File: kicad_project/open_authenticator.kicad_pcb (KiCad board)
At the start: 2 copper layers, 82 x 42 mm, 64 parts, among them IC1 TPS22919DCKR, J1 Conn_01x02_Female, J2 TYPE-C-31-M-17, J3 Conn_01x02_Female, P1 SSD1306_ribbon, Q1 DMP2305U-7, SW1 UP, SW2 DOWN, SW3 BOOT/SELECT, SW4 RESET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

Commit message: Updated silkscreen with symbols, and a bit of art
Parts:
- added ?: , buzzard_labels, F.Cu at (149.0, 117.4)
- added ?: , buzzard_labels, F.Cu at (134.4, 117.4)
- added ?: , buzzard_labels, F.Cu at (124.1, 117.4)
- added ?: , buzzard_labels, F.Cu at (111.7, 117.4)
- added ?: , buzzard_labels, F.Cu at (166.1, 111.5)
- added ?: , buzzard_labels, F.Cu at (166.4, 101.2)
- added ?: , buzzard_labels, F.Cu at (115.0, 95.8)
- added ?: , buzzard_labels, F.Cu at (115.0, 88.8)
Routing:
- net GND: track 213.1 -> 205.0 mm
- net /A1_7_BATT: track 32.5 -> 35.2 mm
- net +3V3: track 139.4 -> 138.2 mm, vias 19 -> 21
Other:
- board text added: "Boot + Reset to flash"
- board text added: "ESP32"
- board text added: "Selects which power source to use"
- board text added: "USB-C"
- board text added: "WiFi Module"
- board text removed: "OFF"
- board text removed: "ON"
- board text removed: "RX"
- board text removed: "TX"

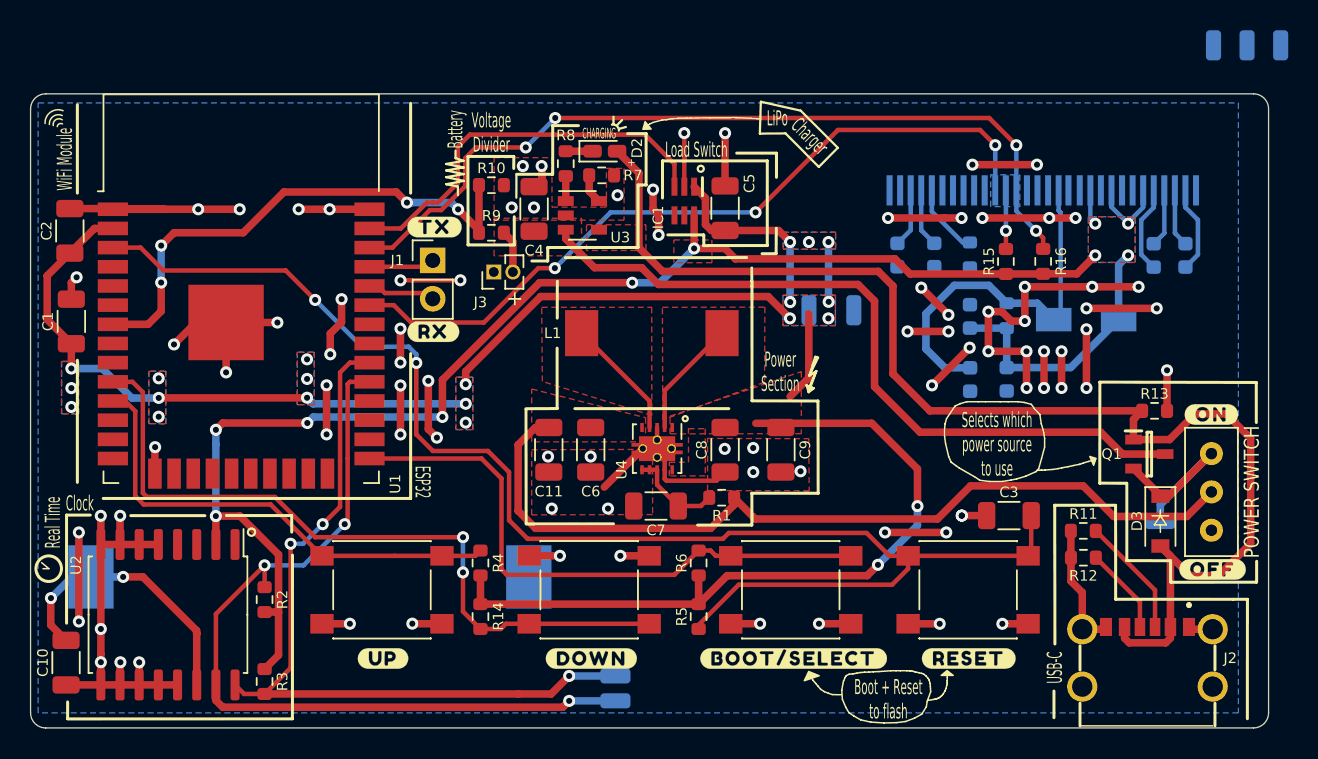
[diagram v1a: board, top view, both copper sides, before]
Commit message: Completed work on F.Cu Layer and F.Silk
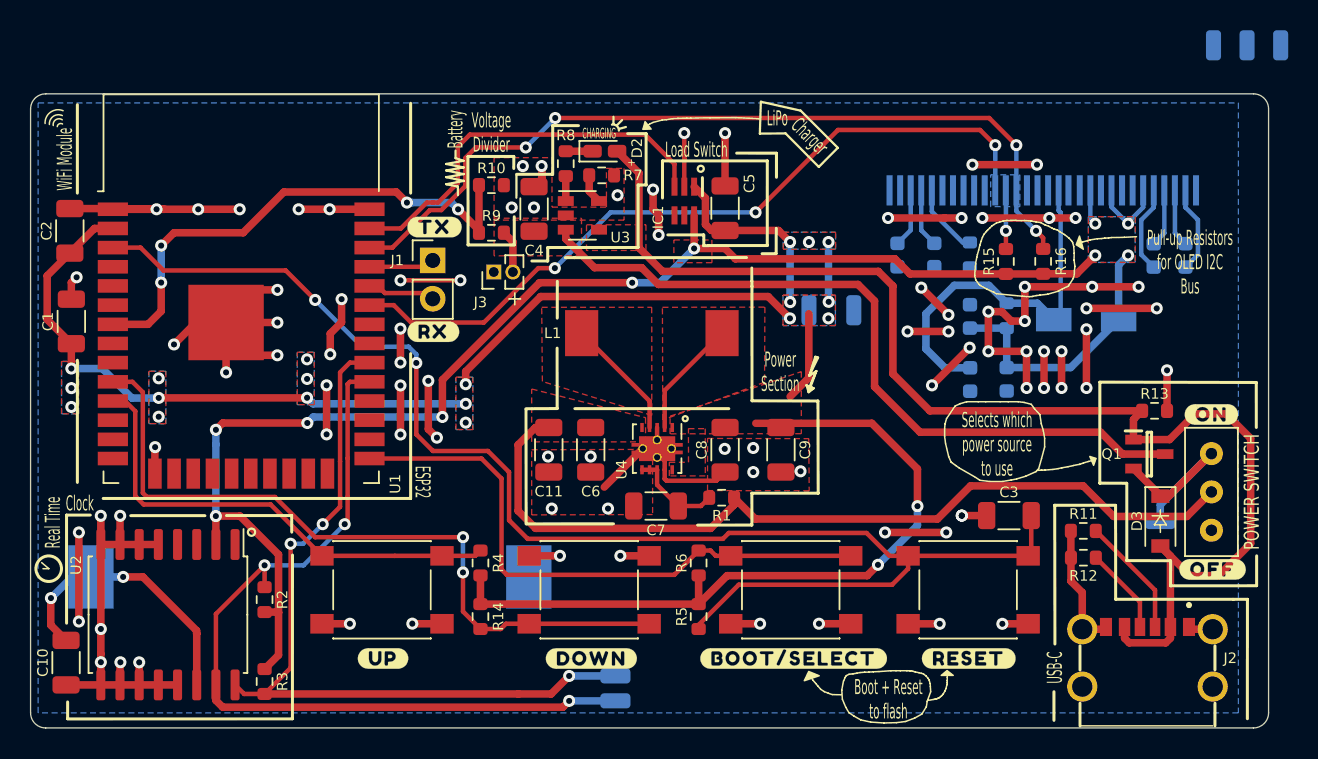
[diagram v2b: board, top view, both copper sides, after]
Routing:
- net GND: track 205.0 -> 214.0 mm, vias 88 -> 91
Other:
- board text added: "Pull-up Resistors for OLED I2C Bus"

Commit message: Placed mounting holes on the board
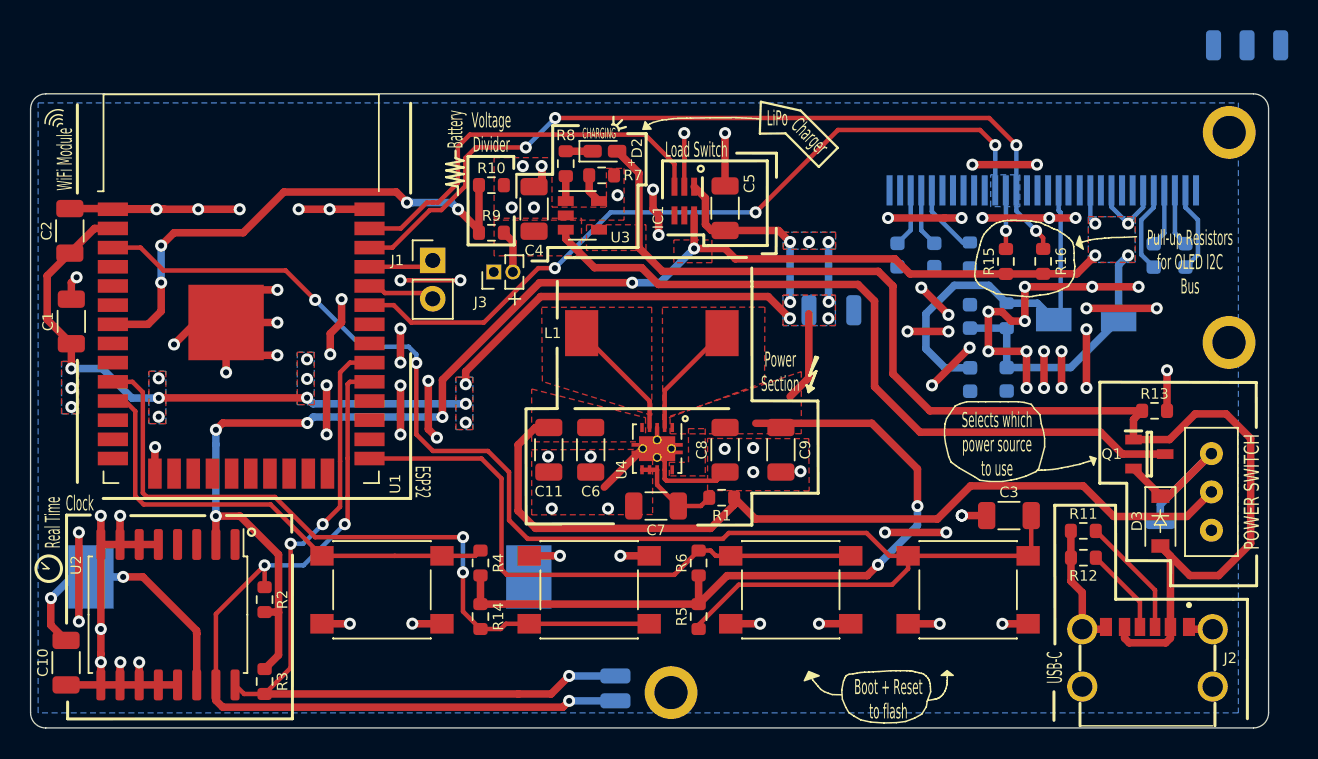
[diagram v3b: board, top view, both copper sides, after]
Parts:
- removed ? (x8): , buzzard_labels
- added H1: MountingHole_Pad, MountingHole:MountingHole_2.2mm_M2_ISO7380_Pad, F.Cu at (169.4, 82.6)
- added H2: MountingHole_Pad, MountingHole:MountingHole_2.2mm_M2_ISO7380_Pad, F.Cu at (169.4, 96.5)
- added H3: MountingHole_Pad, MountingHole:MountingHole_2.2mm_M2_ISO7380_Pad, F.Cu at (132.4, 119.7)

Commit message: ad
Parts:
- added ?: , buzzard_labels, F.Cu at (114.8, 88.8)
- added ?: , buzzard_labels, B.Cu at (141.5, 99.8)
- added ?: , buzzard_labels, B.Cu at (163.2, 108.3)
- added ?: , buzzard_labels, B.Cu at (125.1, 120.2)
- added ?: , buzzard_labels, B.Cu at (125.1, 118.6)
- added ?: , buzzard_labels, F.Cu at (114.9, 95.9)
- added ?: , buzzard_labels, F.Cu at (166.1, 111.6)
- added ?: , buzzard_labels, F.Cu at (166.5, 101.1)
- added ?: , buzzard_labels, F.Cu at (149.0, 117.2)
- added ?: , buzzard_labels, F.Cu at (134.2, 117.2)
- added ?: , buzzard_labels, F.Cu at (124.0, 117.2)
- added ?: , buzzard_labels, F.Cu at (111.6, 117.2)
- added ?: , buzzard_labels, B.Cu at (144.5, 100.0)
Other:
- board text added: "Backup Power for RTC"
- board text added: "CR2032"

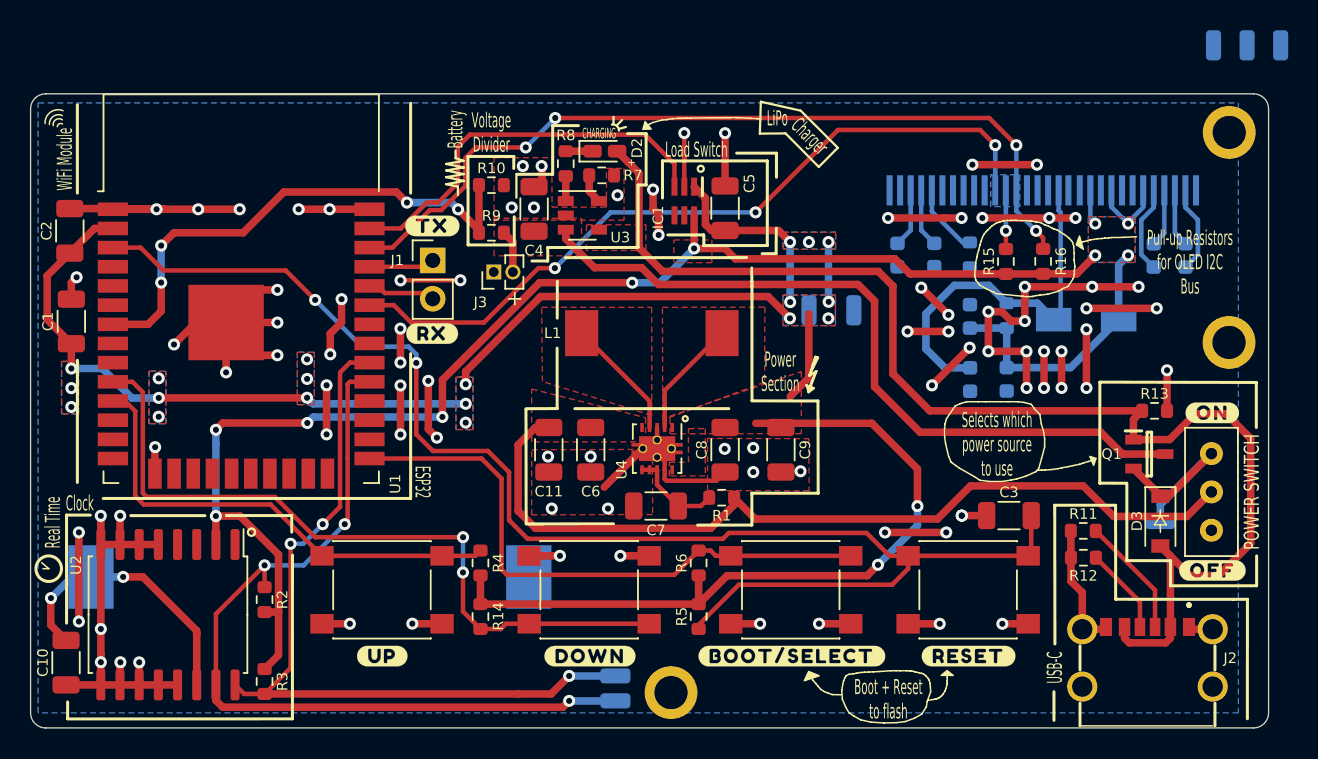
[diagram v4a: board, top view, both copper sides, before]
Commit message: Finished cleaning up bottom layer, silkscreen also updated
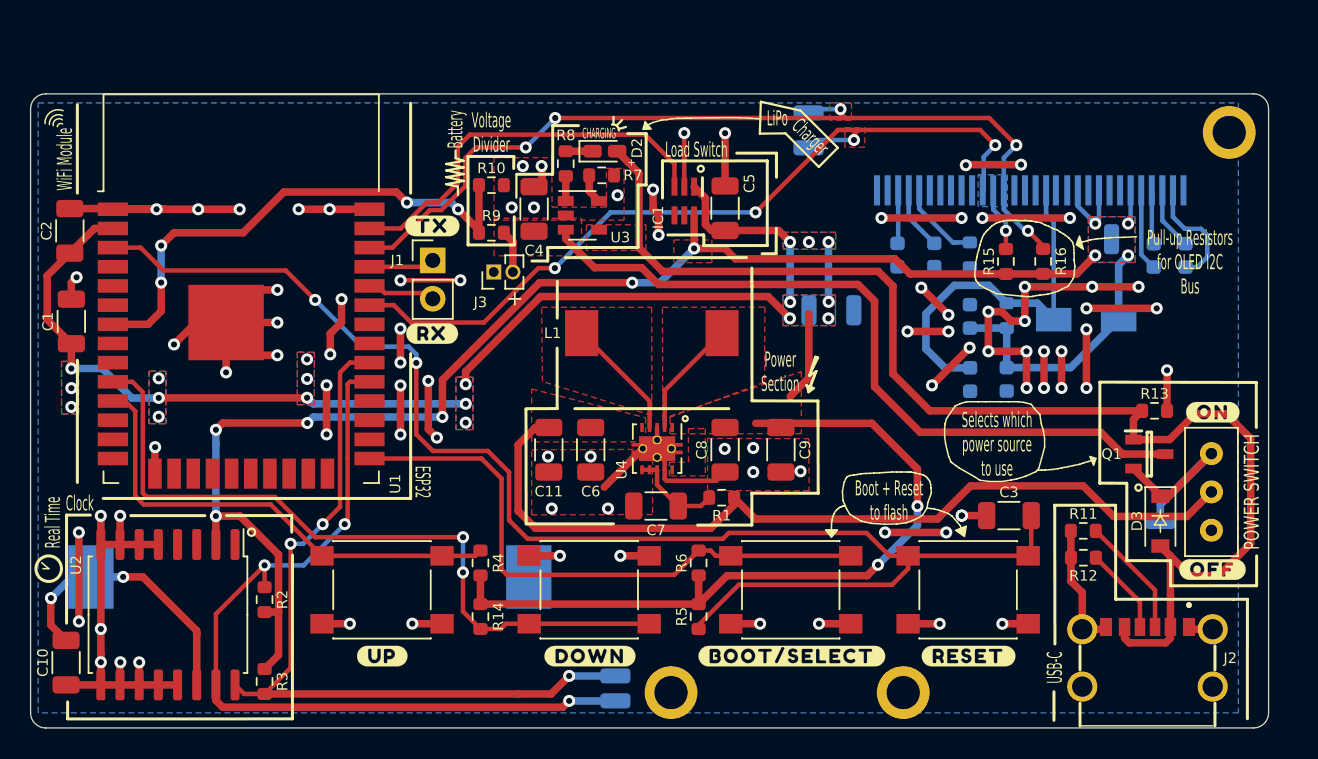
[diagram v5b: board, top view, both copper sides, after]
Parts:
- added ?: , buzzard_labels, B.Cu at (140.2, 83.6)
- added ?: , buzzard_labels, B.Cu at (140.2, 81.3)
- added ?: , buzzard_labels, B.Cu at (161.0, 89.6)
- added REF**: WEEE-Logo_4.2x6mm_SilkScreen, Symbol:WEEE-Logo_4.2x6mm_SilkScreen, B.Cu at (164.0, 117.2)
- added REF**: KiCad-Logo2_5mm_SilkScreen, Symbol:KiCad-Logo2_5mm_SilkScreen, B.Cu at (104.6, 83.2)
- added REF**: OSHW-Logo2_7.3x6mm_SilkScreen, Symbol:OSHW-Logo2_7.3x6mm_SilkScreen, B.Cu at (93.7, 83.4)
- moved H2 31.7 mm to (147.8, 119.7)
- moved TP6 29.8 mm to (141.5, 83.6), turned to 270 degrees
- moved TP7 27.2 mm to (141.5, 81.3), turned to 270 degrees
- moved TP4 17.0 mm to (161.6, 89.6)
- moved P1 0.83 mm to (156.2, 86.4)
- moved ? 0.06 mm to (166.1, 111.5)
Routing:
- net /IO21_SDA: track 54.5 -> 59.2 mm, vias 4 -> 5
- net /IO22_SCL: track 55.8 -> 59.6 mm, vias 4 -> 5
- net Net-(C17-Pad1): track 5.76 -> 7.70 mm
- net Net-(P1-Pad26): track 4.77 -> 5.50 mm
- net Net-(C14-Pad2): track 24.8 -> 25.4 mm
- net GND: track 214.0 -> 213.4 mm, vias 91 -> 90
- added copper zone on F.Cu, net /IO21_SDA
- added copper zone on F.Cu, net /IO22_SCL
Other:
- board text added: "SSD1306 OLED Section"
- board text removed: "Open Authenticator"
- board text removed: "v1.3 Vedant Paranjape"

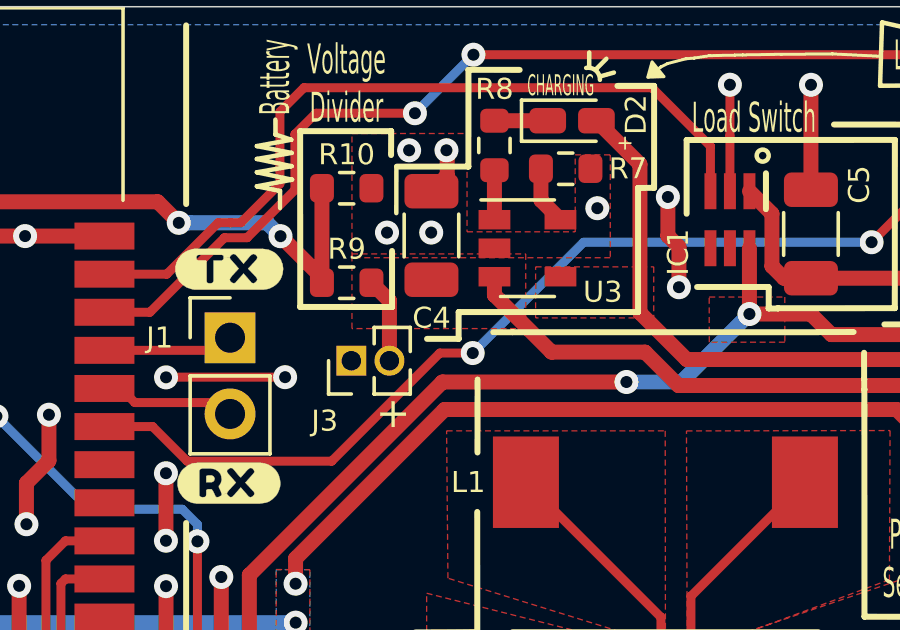
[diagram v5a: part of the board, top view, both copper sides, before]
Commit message: Added lipo connector to board and placed it accordingly
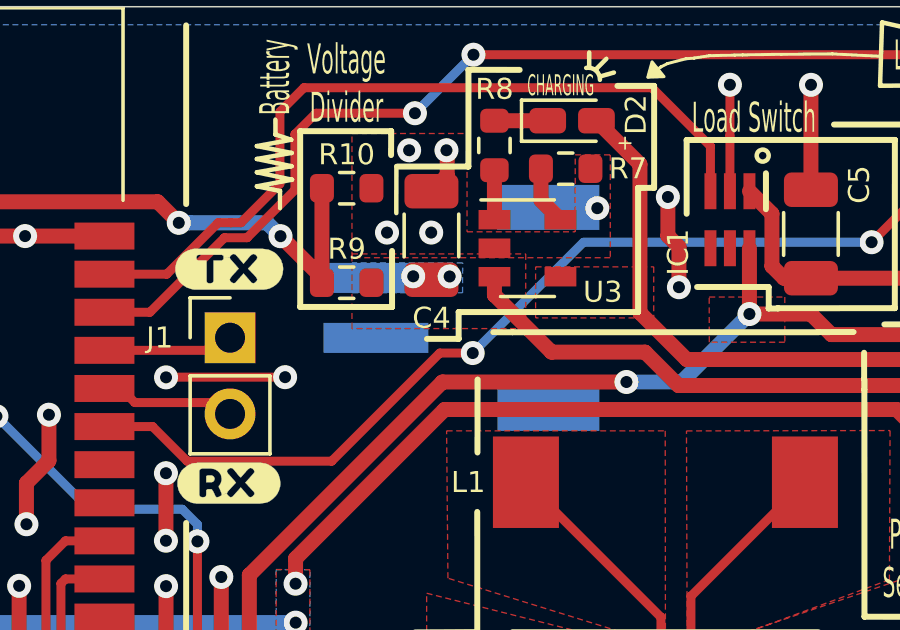
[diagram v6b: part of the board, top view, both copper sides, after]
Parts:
- J3: value Conn_01x02_Female -> S2B-PH-SM4-TB(LF)(SN); footprint Connector_PinHeader_1.27mm:PinHeader_1x02_P1.27mm_Vertical -> jst-ph-2-pin-connector:JST_S2B-PH-SM4-TB(LF)(SN); moved to B.Cu
- moved J3 1.94 mm to (121.5, 90.0), turned to 270 degrees
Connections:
- J3 pad 1: GND -> +BATT
- J3 pad 2: +BATT -> GND
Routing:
- net +BATT: track 52.7 -> 49.8 mm, vias 0 -> 2
- added copper zone on B.Cu, net +BATT
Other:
- board text added: "LiPo Connector"

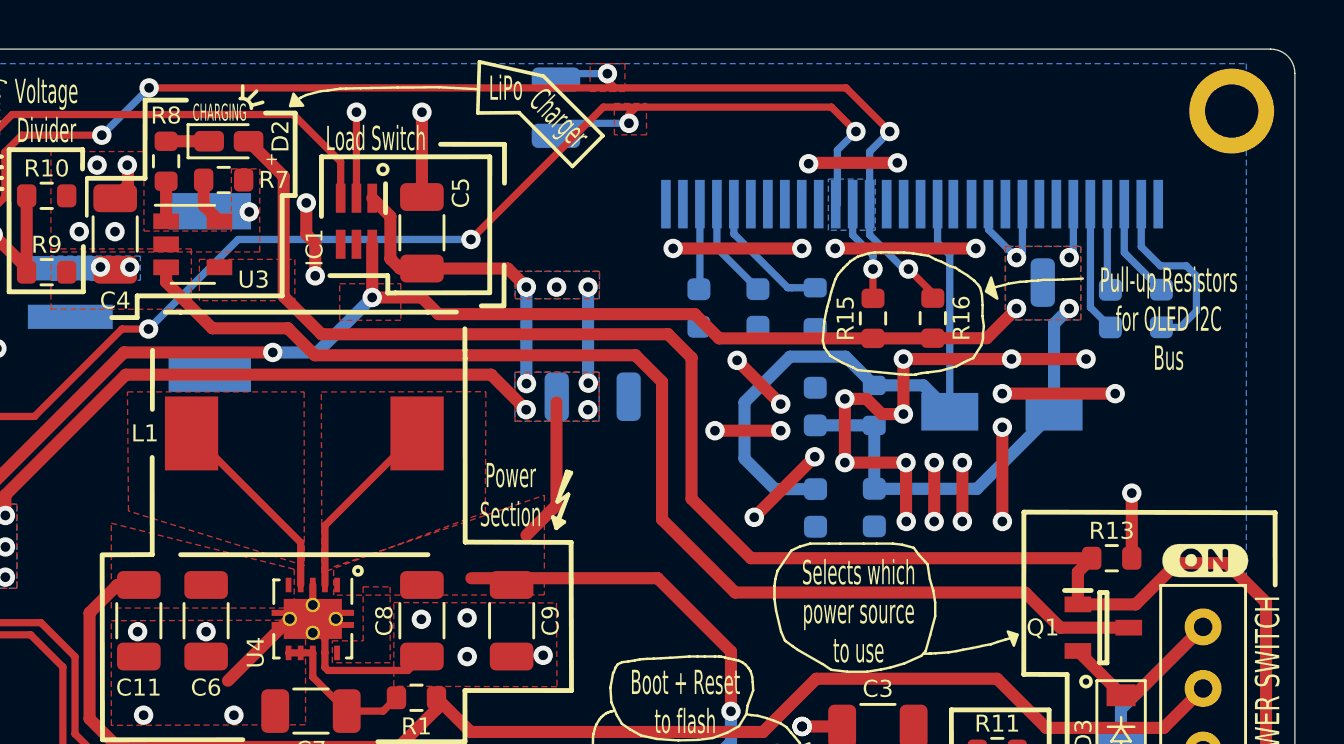
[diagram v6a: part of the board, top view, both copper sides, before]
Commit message: Moved oled subcircuit so as to better fit the OLED on board
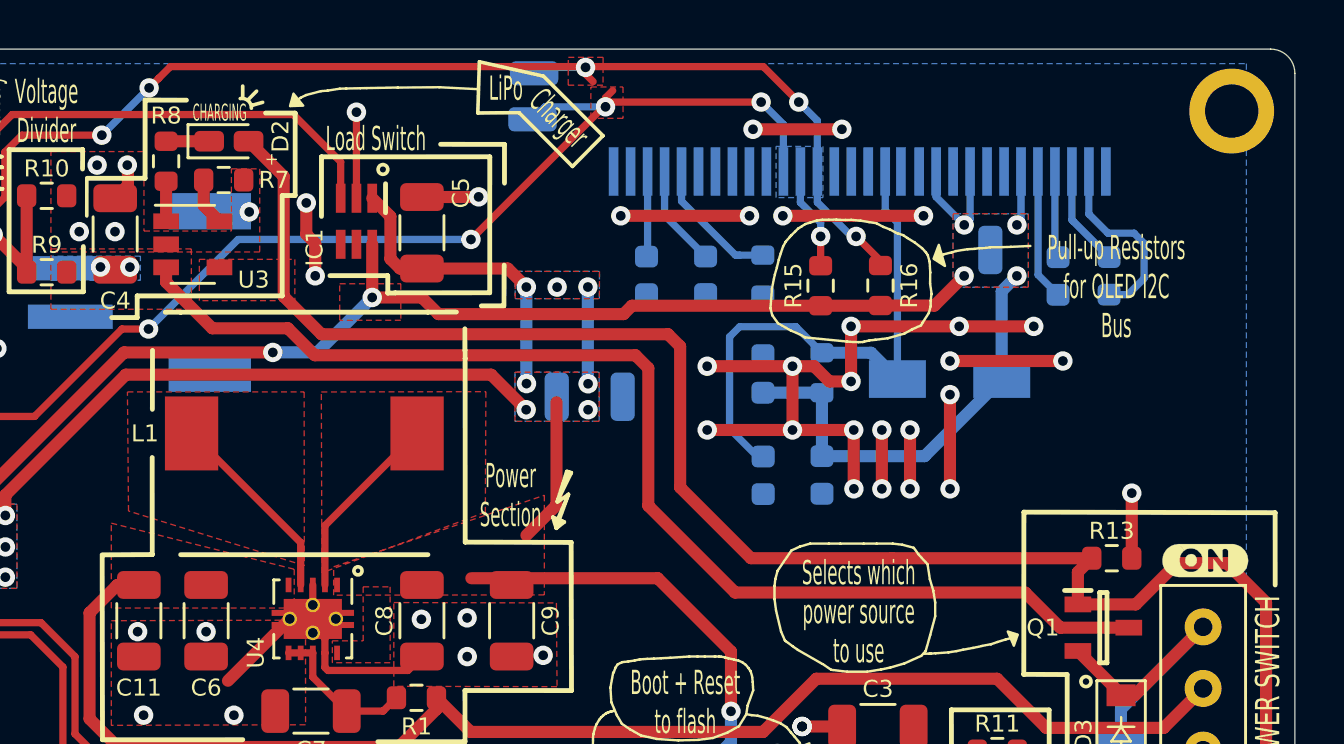
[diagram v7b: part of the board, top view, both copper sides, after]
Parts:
- moved C17 2.54 mm to (164.3, 89.4)
- moved ? 2.54 mm to (158.8, 88.3)
- moved C13 2.54 mm to (152.5, 97.6)
- moved C16 2.54 mm to (145.3, 89.3)
- moved R16 2.54 mm to (154.9, 89.8)
- moved P1 2.54 mm to (154.1, 85.0)
- moved R17 2.54 mm to (152.5, 93.3)
- moved C12 2.54 mm to (150.1, 93.4)
- moved C14 2.54 mm to (150.1, 97.6)
- moved C15 2.54 mm to (147.7, 89.3)
- moved C18 2.54 mm to (162.2, 89.4)
- moved D1 2.54 mm to (157.8, 93.6)
- moved R15 2.54 mm to (152.4, 89.8)
- moved R19 2.54 mm to (150.1, 89.3)
- moved TP4 2.54 mm to (159.4, 88.3)
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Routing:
- net /IO21_SDA: track 59.2 -> 54.9 mm
- net /IO22_SCL: track 59.6 -> 55.9 mm
- net GND: track 213.4 -> 210.5 mm, vias 90 -> 86
- net /LOAD_SWITCH_VCC: track 115.4 -> 112.9 mm
- net Net-(C14-Pad2): track 25.4 -> 23.1 mm
